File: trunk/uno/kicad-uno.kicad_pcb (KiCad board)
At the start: 2 copper layers, 68.6 x 53.3 mm, 54 parts, among them J1 RESET_EN, Q1 FDN340P, SW1 RESET, U1 NCP1117 5V, U2 LP2985-33DBVR, U3 ATMEGA16U2-MU(R), U5 LM358, X1 CSTCE16M0V53 16MHz

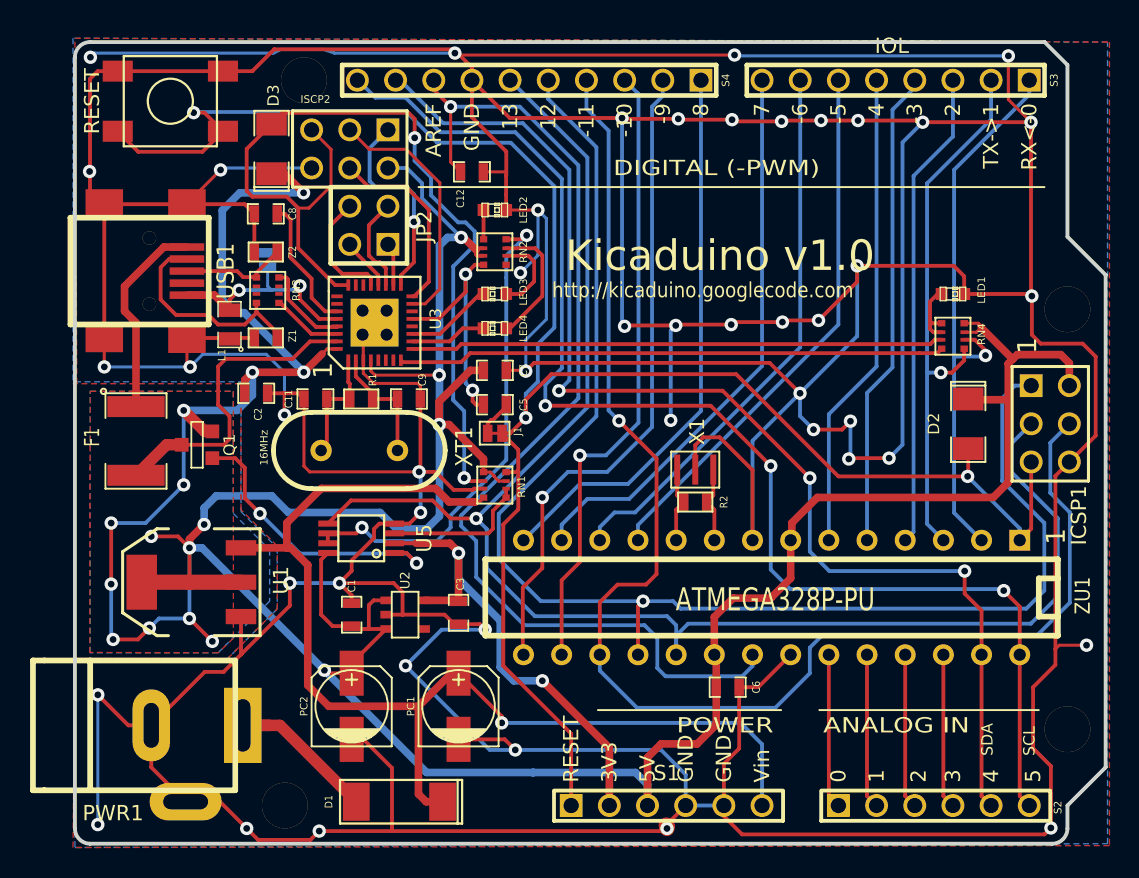
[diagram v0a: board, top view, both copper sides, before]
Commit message: Changed the resistor networks from 0402 to 0603 size, per the original Arduino UNO reference design (I think!)
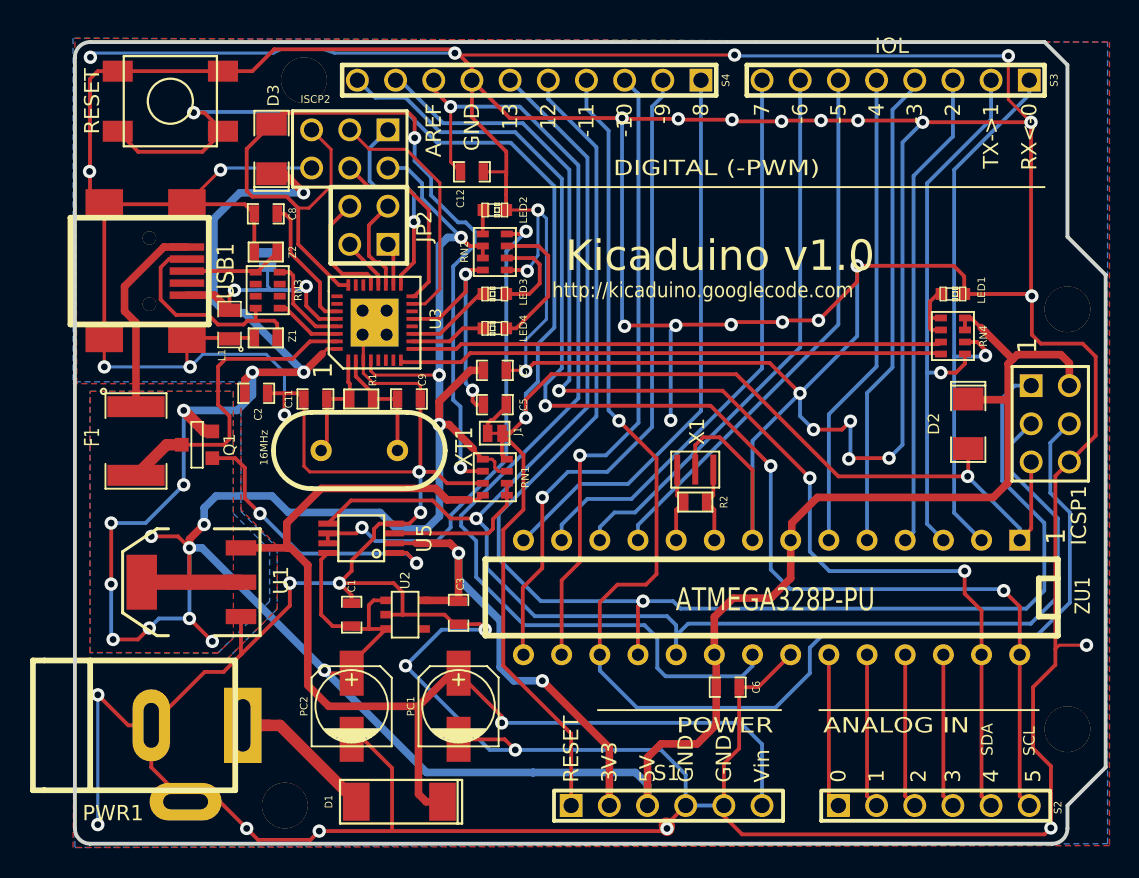
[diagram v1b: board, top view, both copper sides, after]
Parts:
- RN1, RN2, RN3, RN4: footprint RN0402_EXB-2HV -> RN_0603x4
- moved RN1 0.51 mm to (53.3, 54.4)
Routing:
- net /RESET: track 133.9 -> 135.2 mm
- net N-0000062: track 8.61 -> 9.67 mm
- net GND: track 637.4 -> 638.1 mm
- net /USB/RESET2: track 61.2 -> 60.5 mm
- net N-0000060: track 5.56 -> 6.16 mm
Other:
- net class Narrow added: clearance 0.1016, trace_width 0.2032, via_dia 0.889, via_drill 0.635
